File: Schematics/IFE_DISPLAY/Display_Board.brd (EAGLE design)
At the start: 108 x 83.8 mm, 76 parts, among them IC2 EP2C5T144, Q1 16MHz, Q2 MMBT3904L, Q3 16MHz, U1 MCP1826S-1802E/DB, U10 TPS5420D, U2 EPCS1SI8N, U4 HEX_CONVERTER, U5 HEX_CONVERTER, U9 TPS5420D

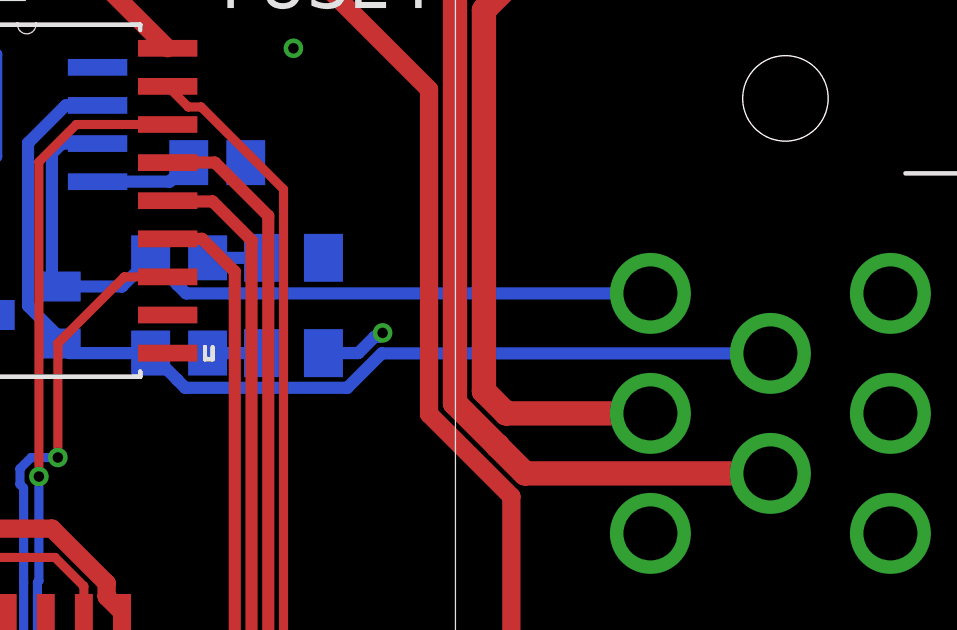
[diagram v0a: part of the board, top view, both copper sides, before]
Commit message: added 120 ohm resistor
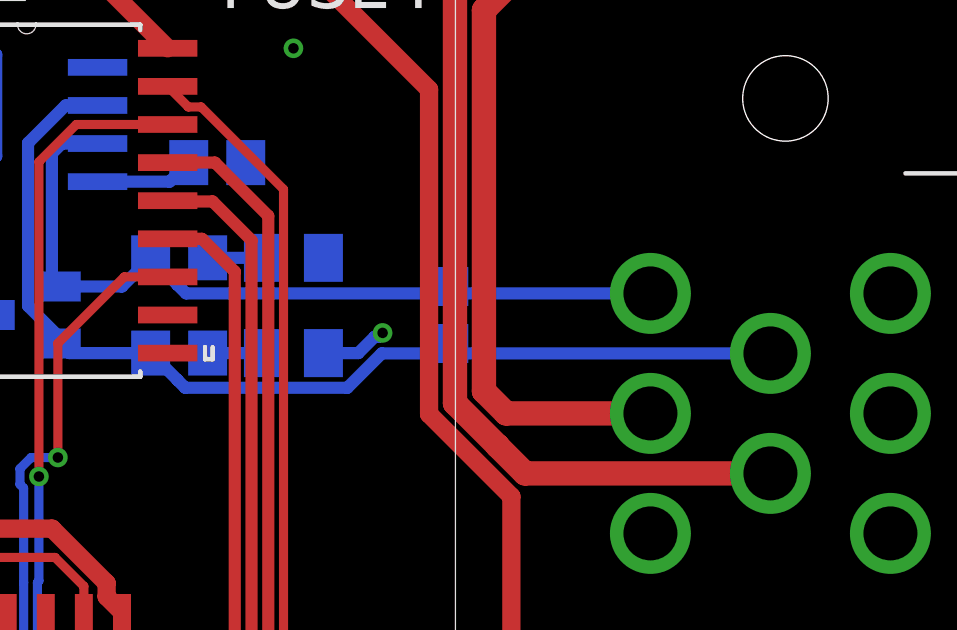
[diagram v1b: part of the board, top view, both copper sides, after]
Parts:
- added R1: 120, rcl:R0805
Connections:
- net CANH: now also R1.1
- net CANL: now also R1.2
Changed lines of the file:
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@@
 <attribute name="OC_NEWARK" value="unknown" x="67.31" y="15.24" size="1.778" layer="28" rot="MR90" display="off"/>
 </element>
+<element name="R1" library="rcl" package="R0805" value="120" x="87.63" y="44.45" rot="MR270"/>
 </elements>
 <signals>
@@
 <wire x1="78.6844" y1="42.2856" x2="78.6844" y2="42.28270625" width="0.4064" layer="16"/>
 <wire x1="84.34729375" y1="42.0244" x2="85.49289375" y2="43.17" width="0.4064" layer="16"/>
-<wire x1="85.49289375" y1="43.17" x2="98.45" y2="43.17" width="0.4064" layer="16"/>
+<wire x1="87.63" y1="43.17" x2="85.49289375" y2="43.17" width="0.4064" layer="16"/>
+<wire x1="87.63" y1="43.17" x2="98.45" y2="43.17" width="0.4064" layer="16"/>
 <wire x1="78.6844" y1="42.28270625" x2="78.94270625" y2="42.0244" width="0.4064" layer="16"/>
 <wire x1="78.94270625" y1="42.0244" x2="84.34729375" y2="42.0244" width="0.4064" layer="16"/>
+<contactref element="R1" pad="2"/>
+<wire x1="87.63" y1="43.5" x2="87.63" y2="43.17" width="0.1524" layer="16"/>
 </signal>
 <signal name="CANH">
@@
 <wire x1="78.6844" y1="45.45770625" x2="78.6844" y2="45.4606" width="0.4064" layer="16"/>
 <wire x1="78.6844" y1="45.4606" x2="77.79" y2="46.355" width="0.4064" layer="16"/>
-<wire x1="94.45" y1="45.17" x2="78.97210625" y2="45.17" width="0.4064" layer="16"/>
+<wire x1="87.63" y1="45.17" x2="94.45" y2="45.17" width="0.4064" layer="16"/>
+<wire x1="87.63" y1="45.17" x2="78.97210625" y2="45.17" width="0.4064" layer="16"/>
 <wire x1="78.97210625" y1="45.17" x2="78.6844" y2="45.45770625" width="0.4064" layer="16"/>
+<contactref element="R1" pad="1"/>
+<wire x1="87.63" y1="45.4" x2="87.63" y2="45.17" width="0.1524" layer="16"/>
 </signal>
 <signal name="N$6">

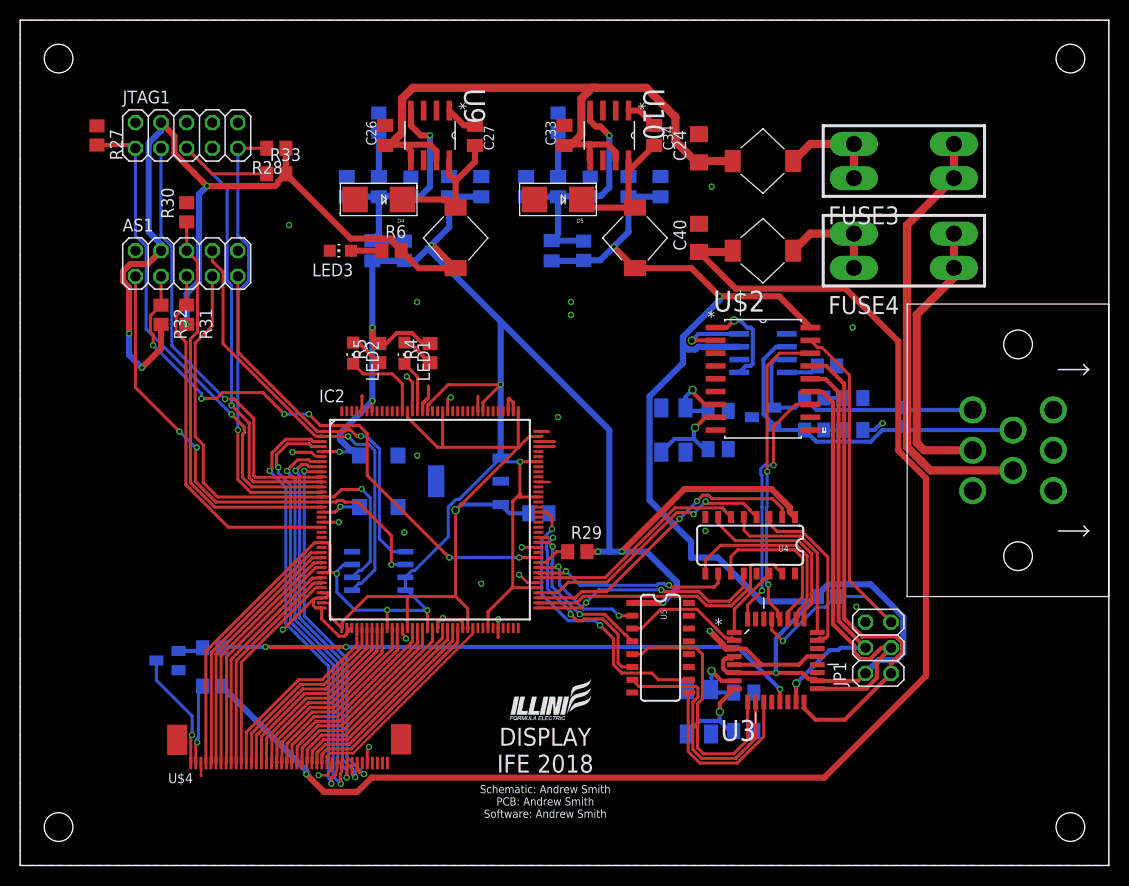
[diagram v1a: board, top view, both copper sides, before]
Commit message: Redid the Switching Supplies
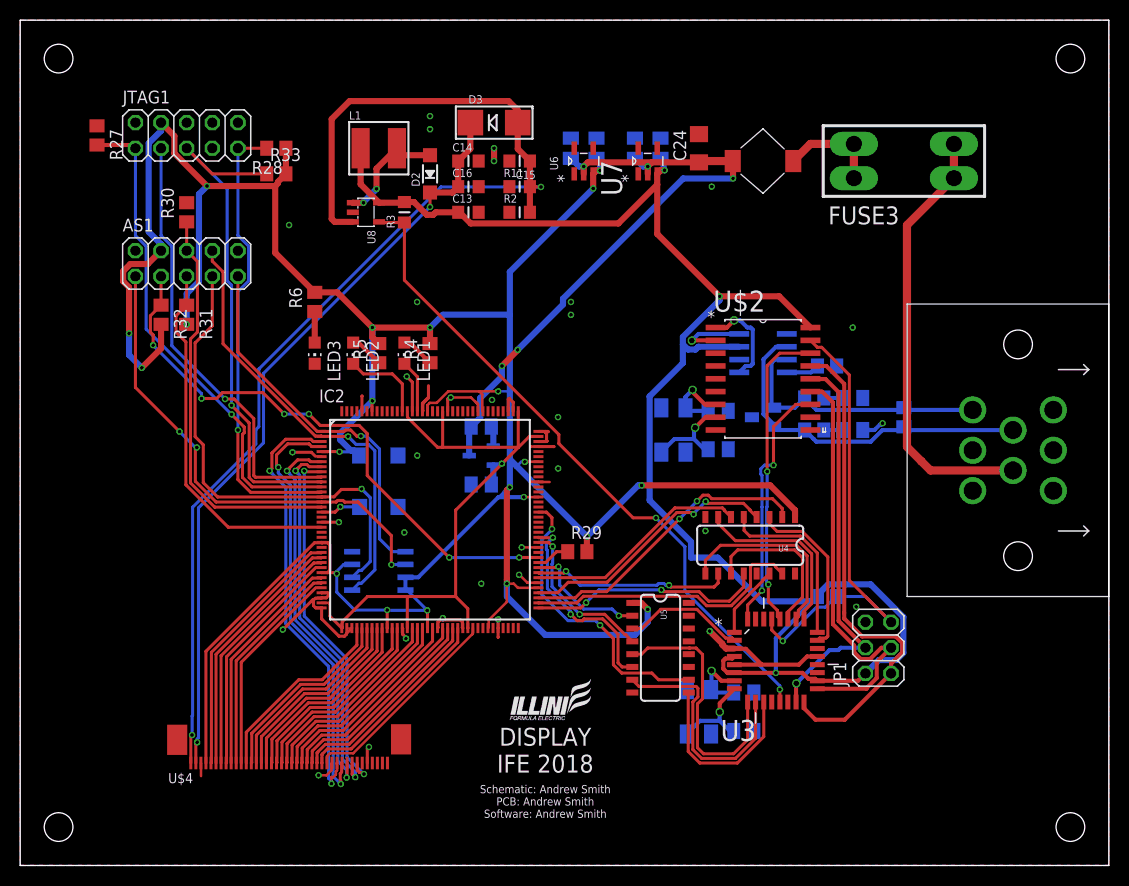
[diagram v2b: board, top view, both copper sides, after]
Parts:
- removed C25: 0.1u, rcl:C0805K
- removed C26, C33: 4.7uF, resistor:C0805K
- removed C27, C34: 0.01uF, resistor:C0805K
- removed C28, C29, C35, C36: 47uF, rcl:C0805K
- removed C30, C37: 1800pF, rcl:C0805K
- removed C31, C38: 0.1uF, rcl:C0805K
- removed C32, C39: 150pF, rcl:C0805K
- removed C40: 220u, Capacitors:C1206
- removed D4, D5: (no value), adafruit:SMADIODE
- removed FUSE4: MINI297-3568, Fuse:3568
- removed L6: 23uH, Inductors:MSS7348
- removed L7: 58uH, Inductors:MSS7348
- removed L8: 20uH, Inductors:MSS7348
- removed Q2: MMBT3904L, transistor-npn:SOT23-BEC
- removed R12: 5.9k, rcl:R0805
- removed R13, R36: 549, rcl:R0805
- removed R25: 76, resistor:R0805
- removed R26: 5.2k, resistor:R0805
- removed R34: 10k, rcl:R0805
- removed R35: 3.2k, rcl:R0805
- removed U1: MCP1826S-1802E/DB, Microchip_By_element14_Batch_1:SOT230P700X180-4N
- removed U10, U9: TPS5420D, Texas Instruments_By_element14_Batch_1:SOIC127P600X175-8N
- added C1, C2: 1uF, rcl:C0805K
- added C10, C11, C12, C5: 0.1u, rcl:C0805K
- added C13: 10uF, microbuilder:_0805MP
- added C14, C16: 1uF, microbuilder:_0805MP
- added C15: 0.1uF, microbuilder:_0805MP
- added D2: MBR0540, microbuilder:SOD-123
- added D3: MM3Z24VT1G, microbuilder:SMADIODE
- added L1: 6.8uH power L CID 2276, microbuilder:INDUCTOR_5X5MM_NR5040_NOTHERMALS
- added R11: 6Ω, microbuilder:_0805MP
- added R2: 12Ω, microbuilder:_0805MP
- added U$5: MCP1702T-1202E/CB, Microchip_By_element14_Batch_1:SOT95P300X145-3N
- added U6: MC78LC33NTRG, ON Semiconductor_By_element14_Batch_1:SOT95P275X110-5N
- added U7: MC78LC50NTRG, ON Semiconductor_By_element14_Batch_1:SOT95P275X110-5N
- added U8: FAN5333BSX, microbuilder:SOT23-5@1
- R3: value 10k -> 10K; device rcl:R0805 -> microbuilder:_0805MP
- moved LED3 10.5 mm to (29.2, 50.8), turned to 180 degrees
- moved R6 9.16 mm to (29.2, 55.9), turned to 90 degrees
- moved R3 3.81 mm to (38.1, 64.8), flipped to the top, turned to 90 degrees
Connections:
- removed net +24V: C40.1, L8.P$2, R25.2
- removed net N$13: Q2.B, R26.1
- removed net N$22: C27.1, U9.1
- removed net N$23: C27.2, D4.C, L6.P$1, U9.8
- removed net N$25: C30.2, C31.1, C32.1, R12.2, R3.1, U9.4
- removed net N$26: C31.2, R13.2
- removed net N$27: C34.1, U10.1
- removed net N$28: C34.2, D5.C, L7.P$1, U10.8
- removed net N$30: C37.2, C38.1, C39.1, R34.1, R35.2, U10.4
- removed net N$31: C38.2, R36.2
- removed net N$32: FUSE4.P$1, FUSE4.P$4, L8.P$1
- new net N$8: D2.A, L1.P$2, U8.1
- net +12V: now also C10.1, C11.1, C2.1, U$5.3, U6.2, U7.2; no longer C26.1, C33.1, U10.5, U10.7, U9.5, U9.7
- net +3V3: now also C12.1, U6.3; no longer C28.1, C29.1, C30.1, L6.P$2, R3.2, U1.1
- net +5V: now also C13.1, C5.1, L1.P$1, R3.2, U7.3, U8.5; no longer C35.1, C36.1, C37.1, L7.P$2, R34.2
- net DISP_LEDA: now also C14.1, C16.1, D2.C, D3.C; no longer R25.1
- net DISP_LEDK: now also C15.1, D3.A, R11.2, R2.2, U8.3; no longer Q2.C
- net DISP_PWM: now also R3.1, U8.4; no longer R26.2
- net GND: now also C1.2, C10.2, C11.2, C12.2, C13.2, C14.2, C15.2, C16.2, C2.2, C5.2, R11.1, R2.1, U$5.1, U6.1, U7.1, U8.2; no longer C25.2, C26.2, C28.2, C29.2, C32.2, C33.2, C35.2, C36.2, C39.2, C40.2, D4.A, D5.A, Q2.E, R12.1, R13.1, R35.1, R36.1, U1.2, U1.4, U10.6, U9.6
- net PWR_IN_24: no longer FUSE4.P$2, FUSE4.P$3
- net VCC: now also C1.1, U$5.2; no longer C25.1, U1.3
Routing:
- net +24V: track 140.5 -> 0.00 mm, vias 1 -> 0
- net DISP_LEDK: track 11.7 -> 120.8 mm, vias 1 -> 2
- net DISP_LEDA: track 7.90 -> 76.1 mm, vias 1 -> 2
- net PWR_IN_24: track 28.7 -> 0.00 mm
- net +5V: track 134.0 -> 159.4 mm
- net N$25: track 25.3 -> 0.00 mm, vias 1 -> 0
- net N$30: track 25.1 -> 0.00 mm, vias 1 -> 0
- net +3V3: track 338.8 -> 322.8 mm, vias 16 -> 21
- net N$23: track 14.9 -> 0.00 mm
- net N$28: track 14.2 -> 0.00 mm
- net N$8: track 0.00 -> 11.4 mm, vias 0 -> 2
- net N$32: track 10.1 -> 0.00 mm
- net DISP_PWM: track 58.4 -> 66.8 mm, vias 3 -> 2
- net GND: track 72.7 -> 80.7 mm, vias 25 -> 31
- net N$31: track 4.40 -> 0.00 mm
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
